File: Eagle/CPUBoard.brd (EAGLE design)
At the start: 100 x 80 mm, 33 parts, among them IC2 MAX232, IC3 MAX485CPA, J1 DISPLAY, J2 BUTTON_BOARD, J3 RELAY_BOARD, Q1 12.000MHz, X6 MKDSN1,5/3-5,08, X7 MKDSN1,5/3-5,08

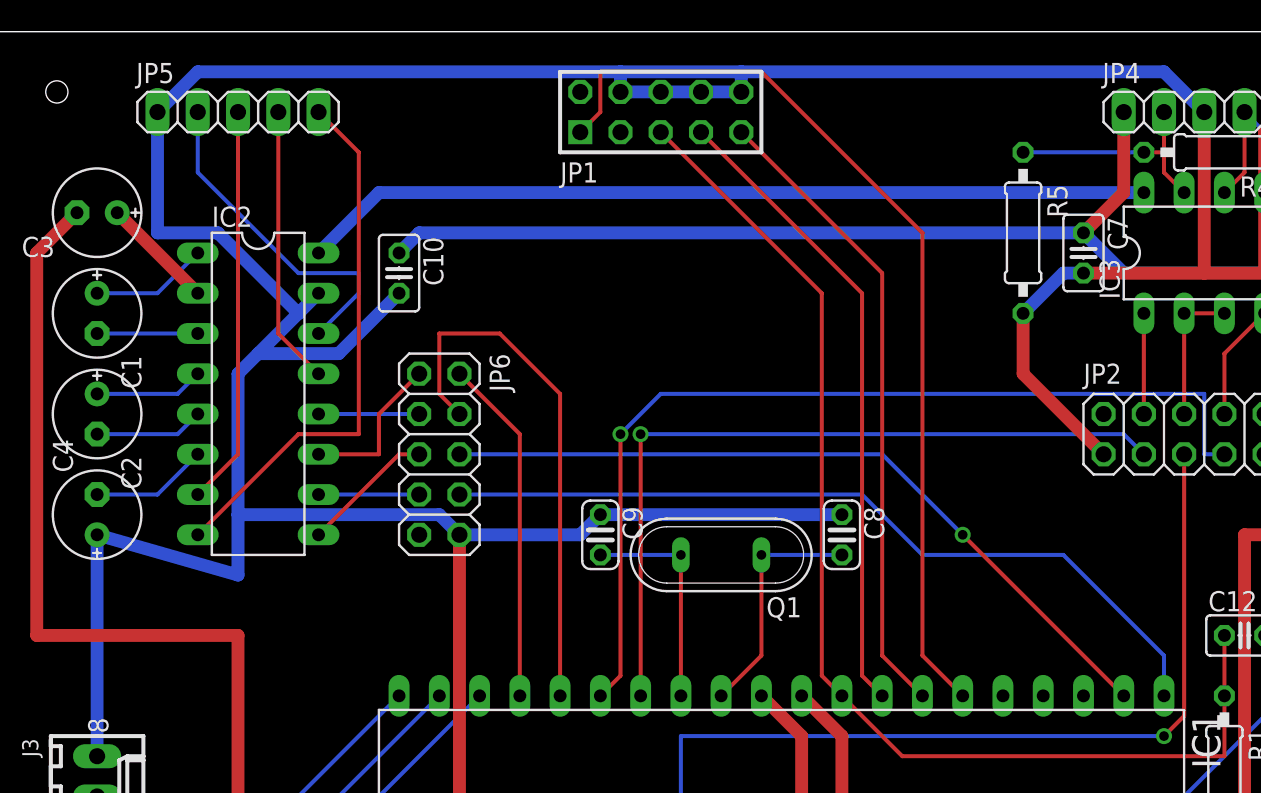
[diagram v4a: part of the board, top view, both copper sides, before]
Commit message: - wiring from/to MAX232 changed slightly
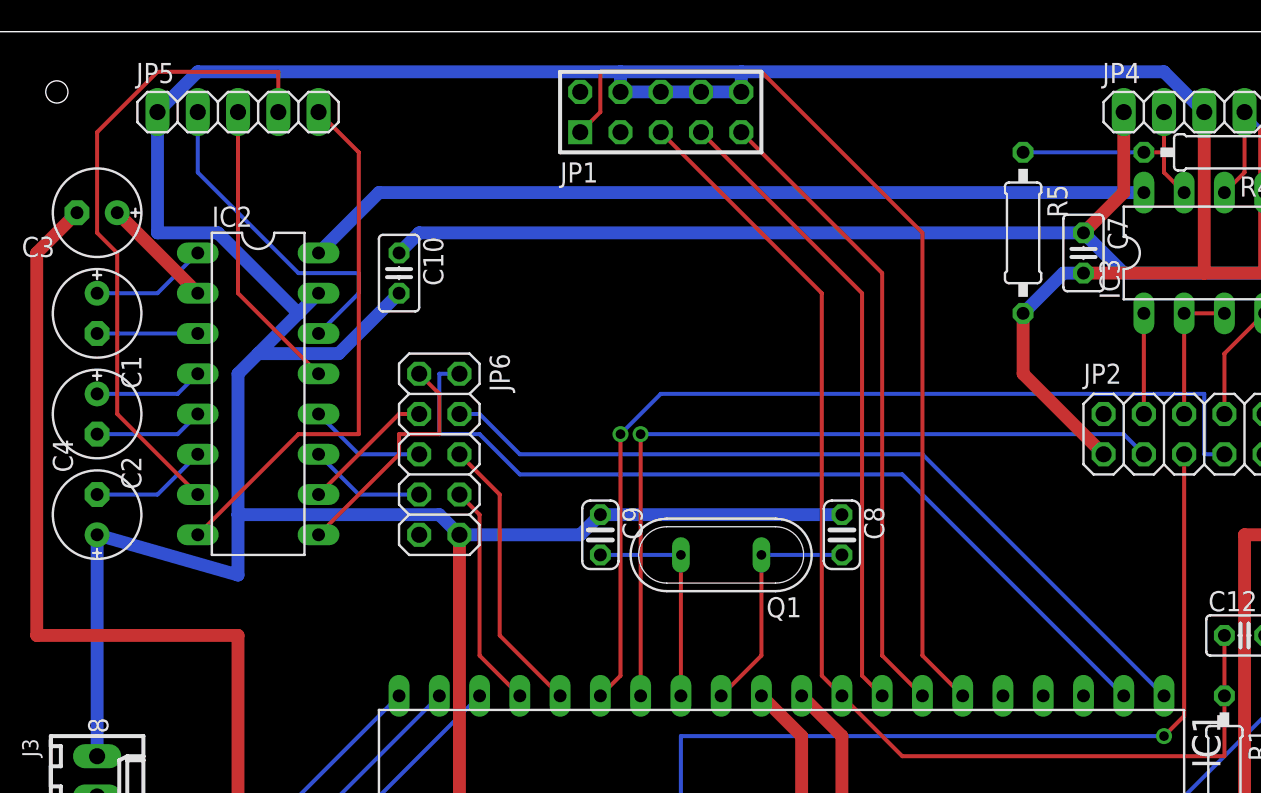
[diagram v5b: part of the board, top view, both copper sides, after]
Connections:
- removed net N$30: IC1.2, JP6.6
- removed net N$31: IC1.1, JP6.8
- new net N$22: IC1.16, JP6.6
- new net N$25: IC1.2, JP6.2
- net N$11: now also JP6.5; no longer JP6.3
- net N$16: now also IC1.1; no longer IC1.16
- net N$24: now also JP6.8; no longer JP6.2
- net N$28: now also JP6.1; no longer JP6.5
- net N$29: now also JP6.3; no longer JP6.7
- net N$4: now also JP6.7; no longer JP6.1
- net SER1_CTS: now also IC2.13; no longer IC2.7
- net SER1_RXD: now also IC2.7; no longer IC2.13
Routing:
- net N$25: track 0.00 -> 55.1 mm
- net N$31: track 51.2 -> 0.00 mm
- net N$30: track 48.2 -> 0.00 mm, vias 1 -> 0
- net SER1_RXD: track 17.6 -> 41.0 mm
- net N$16: track 33.9 -> 51.8 mm
- net N$22: track 0.00 -> 17.9 mm
- net N$24: track 21.9 -> 14.3 mm
- net N$28: track 8.45 -> 15.3 mm
- net SER1_CTS: track 25.2 -> 18.6 mm
- net N$4: track 9.94 -> 7.40 mm
- net N$29: track 6.35 -> 8.45 mm
- net N$11: track 6.35 -> 7.40 mm
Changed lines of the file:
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@@
 <wire x1="12.7" y1="74.93" x2="12.7" y2="71.12" width="0.254" layer="16"/>
 </signal>
-<signal name="SER1_RXD">
+<signal name="SER1_CTS">
 <contactref element="IC2" pad="13"/>
-<contactref element="JP5" pad="4"/>
-<wire x1="17.78" y1="60.96" x2="20.32" y2="58.42" width="0.254" layer="1"/>
-<wire x1="17.78" y1="74.93" x2="17.78" y2="60.96" width="0.254" layer="1"/>
+<contactref element="JP5" pad="3"/>
+<wire x1="15.24" y1="63.5" x2="20.32" y2="58.42" width="0.254" layer="1"/>
+<wire x1="15.24" y1="74.93" x2="15.24" y2="63.5" width="0.254" layer="1"/>
 </signal>
 <signal name="ENC_SCK">
@@
 <wire x1="38.1" y1="74.93" x2="38.1" y2="77.47" width="0.254" layer="1"/>
 <wire x1="36.83" y1="73.66" x2="38.1" y2="74.93" width="0.254" layer="1"/>
-</signal>
-<signal name="SER1_CTS">
-<contactref element="IC2" pad="7"/>
-<contactref element="JP5" pad="3"/>
-<wire x1="15.24" y1="53.34" x2="12.7" y2="50.8" width="0.254" layer="1"/>
-<wire x1="15.24" y1="74.93" x2="15.24" y2="53.34" width="0.254" layer="1"/>
 </signal>
 <signal name="LED_GREEN">
@@
 <signal name="N$4">
 <contactref element="IC2" pad="11"/>
-<contactref element="JP6" pad="1"/>
-<wire x1="24.13" y1="53.34" x2="20.32" y2="53.34" width="0.254" layer="1"/>
-<wire x1="24.13" y1="55.88" x2="24.13" y2="53.34" width="0.254" layer="1"/>
-<wire x1="26.67" y1="58.42" x2="24.13" y2="55.88" width="0.254" layer="1"/>
+<contactref element="JP6" pad="7"/>
+<wire x1="22.86" y1="50.8" x2="20.32" y2="53.34" width="0.254" layer="16"/>
+<wire x1="26.67" y1="50.8" x2="22.86" y2="50.8" width="0.254" layer="16"/>
 </signal>
 <signal name="N$11">
 <contactref element="IC2" pad="12"/>
-<contactref element="JP6" pad="3"/>
-<wire x1="26.67" y1="55.88" x2="20.32" y2="55.88" width="0.254" layer="16"/>
+<contactref element="JP6" pad="5"/>
+<wire x1="22.86" y1="53.34" x2="20.32" y2="55.88" width="0.254" layer="16"/>
+<wire x1="26.67" y1="53.34" x2="22.86" y2="53.34" width="0.254" layer="16"/>
 </signal>
 <signal name="N$13">
@@
 <wire x1="72.39" y1="72.39" x2="64.77" y2="72.39" width="0.254" layer="16"/>
 </signal>
-<signal name="N$16">
-<contactref element="IC1" pad="16"/>
-<contactref element="JP6" pad="4"/>
-<wire x1="35.56" y1="38.1" x2="35.56" y2="57.15" width="0.254" layer="1"/>
-<wire x1="35.56" y1="57.15" x2="31.75" y2="60.96" width="0.254" layer="1"/>
-<wire x1="31.75" y1="60.96" x2="27.94" y2="60.96" width="0.254" layer="1"/>
-<wire x1="27.94" y1="60.96" x2="27.94" y2="57.15" width="0.254" layer="1"/>
-<wire x1="27.94" y1="57.15" x2="29.21" y2="55.88" width="0.254" layer="1"/>
-</signal>
 <signal name="N$28">
 <contactref element="IC2" pad="9"/>
-<contactref element="JP6" pad="5"/>
+<contactref element="JP6" pad="1"/>
 <wire x1="25.4" y1="53.34" x2="20.32" y2="48.26" width="0.254" layer="1"/>
-<wire x1="26.67" y1="53.34" x2="25.4" y2="53.34" width="0.254" layer="1"/>
+<wire x1="25.4" y1="54.61" x2="25.4" y2="53.34" width="0.254" layer="1"/>
+<wire x1="27.94" y1="54.61" x2="25.4" y2="54.61" width="0.254" layer="1"/>
+<wire x1="27.94" y1="57.15" x2="27.94" y2="54.61" width="0.254" layer="1"/>
+<wire x1="26.67" y1="58.42" x2="27.94" y2="57.15" width="0.254" layer="1"/>
 </signal>
 <signal name="N$29">
 <contactref element="IC2" pad="10"/>
-<contactref element="JP6" pad="7"/>
-<wire x1="26.67" y1="50.8" x2="20.32" y2="50.8" width="0.254" layer="16"/>
-</signal>
-<signal name="N$30">
-<contactref element="IC1" pad="2"/>
-<contactref element="JP6" pad="6"/>
-<wire x1="60.96" y1="48.26" x2="71.12" y2="38.1" width="0.254" layer="1"/>
-<wire x1="55.88" y1="53.34" x2="60.96" y2="48.26" width="0.254" layer="16"/>
-<wire x1="29.21" y1="53.34" x2="55.88" y2="53.34" width="0.254" layer="16"/>
-<via x="60.96" y="48.26" extent="1-16" drill="0.6096"/>
-</signal>
-<signal name="N$31">
-<contactref element="IC1" pad="1"/>
-<contactref element="JP6" pad="8"/>
-<wire x1="73.66" y1="40.64" x2="73.66" y2="38.1" width="0.254" layer="16"/>
-<wire x1="67.31" y1="46.99" x2="73.66" y2="40.64" width="0.254" layer="16"/>
-<wire x1="58.42" y1="46.99" x2="67.31" y2="46.99" width="0.254" layer="16"/>
-<wire x1="54.61" y1="50.8" x2="58.42" y2="46.99" width="0.254" layer="16"/>
-<wire x1="29.21" y1="50.8" x2="54.61" y2="50.8" width="0.254" layer="16"/>
+<contactref element="JP6" pad="3"/>
+<wire x1="25.4" y1="55.88" x2="20.32" y2="50.8" width="0.254" layer="1"/>
+<wire x1="26.67" y1="55.88" x2="25.4" y2="55.88" width="0.254" layer="1"/>
 </signal>
 <signal name="N$24">
 <contactref element="IC1" pad="17"/>
-<contactref element="JP6" pad="2"/>
-<wire x1="33.02" y1="54.61" x2="33.02" y2="38.1" width="0.254" layer="1"/>
-<wire x1="29.21" y1="58.42" x2="33.02" y2="54.61" width="0.254" layer="1"/>
+<contactref element="JP6" pad="8"/>
+<wire x1="30.48" y1="40.64" x2="33.02" y2="38.1" width="0.254" layer="1"/>
+<wire x1="30.48" y1="49.53" x2="30.48" y2="40.64" width="0.254" layer="1"/>
+<wire x1="29.21" y1="50.8" x2="30.48" y2="49.53" width="0.254" layer="1"/>
 </signal>
 <signal name="N$19">
@@
 <contactref element="J1" pad="1"/>
 </signal>
+<signal name="SER1_RXD">
+<contactref element="IC2" pad="7"/>
+<contactref element="JP5" pad="4"/>
+<wire x1="7.62" y1="55.88" x2="12.7" y2="50.8" width="0.254" layer="1"/>
+<wire x1="7.62" y1="66.04" x2="7.62" y2="55.88" width="0.254" layer="1"/>
+<wire x1="6.35" y1="67.31" x2="7.62" y2="66.04" width="0.254" layer="1"/>
+<wire x1="6.35" y1="73.66" x2="6.35" y2="67.31" width="0.254" layer="1"/>
+<wire x1="10.16" y1="77.47" x2="6.35" y2="73.66" width="0.254" layer="1"/>
+<wire x1="17.78" y1="77.47" x2="10.16" y2="77.47" width="0.254" layer="1"/>
+<wire x1="17.78" y1="74.93" x2="17.78" y2="77.47" width="0.254" layer="1"/>
+</signal>
+<signal name="N$22">
+<contactref element="JP6" pad="6"/>
+<contactref element="IC1" pad="16"/>
+<wire x1="31.75" y1="41.91" x2="35.56" y2="38.1" width="0.254" layer="1"/>
+<wire x1="31.75" y1="50.8" x2="31.75" y2="41.91" width="0.254" layer="1"/>
+<wire x1="29.21" y1="53.34" x2="31.75" y2="50.8" width="0.254" layer="1"/>
+</signal>
+<signal name="N$16">
+<contactref element="IC1" pad="1"/>
+<contactref element="JP6" pad="4"/>
+<wire x1="58.42" y1="53.34" x2="73.66" y2="38.1" width="0.254" layer="16"/>
+<wire x1="33.02" y1="53.34" x2="58.42" y2="53.34" width="0.254" layer="16"/>
+<wire x1="30.48" y1="55.88" x2="33.02" y2="53.34" width="0.254" layer="16"/>
+<wire x1="29.21" y1="55.88" x2="30.48" y2="55.88" width="0.254" layer="16"/>
+</signal>
+<signal name="N$25">
+<contactref element="JP6" pad="2"/>
+<contactref element="IC1" pad="2"/>
+<wire x1="57.15" y1="52.07" x2="71.12" y2="38.1" width="0.254" layer="16"/>
+<wire x1="33.02" y1="52.07" x2="57.15" y2="52.07" width="0.254" layer="16"/>
+<wire x1="30.48" y1="54.61" x2="33.02" y2="52.07" width="0.254" layer="16"/>
+<wire x1="27.94" y1="54.61" x2="30.48" y2="54.61" width="0.254" layer="16"/>
+<wire x1="27.94" y1="58.42" x2="27.94" y2="54.61" width="0.254" layer="16"/>
+<wire x1="29.21" y1="58.42" x2="27.94" y2="58.42" width="0.254" layer="16"/>
+</signal>
 </signals>

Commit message: - another fix for the TWI pins, hopefully the last one!
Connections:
- net SCL: now also J1.3; no longer J1.2
- net SDA: now also J1.2; no longer J1.3
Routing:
- net GND: track 393.2 -> 400.4 mm
- net N$14: track 60.0 -> 64.3 mm
- net SCL: track 21.2 -> 23.9 mm
- net SDA: track 23.7 -> 24.7 mm
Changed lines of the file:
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@@
 <wire x1="52.07" y1="21.59" x2="50.8" y2="22.86" width="0.8128" layer="1"/>
 <wire x1="52.07" y1="17.78" x2="52.07" y2="21.59" width="0.8128" layer="1"/>
-<wire x1="50.8" y1="35.56" x2="48.26" y2="38.1" width="0.8128" layer="1"/>
-<wire x1="50.8" y1="22.86" x2="50.8" y2="29.21" width="0.8128" layer="1"/>
-<wire x1="50.8" y1="29.21" x2="50.8" y2="35.56" width="0.8128" layer="1"/>
 <wire x1="46.99" y1="19.05" x2="45.72" y2="17.78" width="0.8128" layer="16"/>
 <wire x1="50.8" y1="19.05" x2="46.99" y2="19.05" width="0.8128" layer="16"/>
@@
 <wire x1="36.83" y1="48.26" x2="38.1" y2="49.53" width="0.8128" layer="16"/>
 <wire x1="29.21" y1="48.26" x2="36.83" y2="48.26" width="0.8128" layer="16"/>
-<wire x1="38.1" y1="49.53" x2="53.34" y2="49.53" width="0.8128" layer="16"/>
+<wire x1="38.1" y1="49.53" x2="43.18" y2="49.53" width="0.8128" layer="16"/>
+<wire x1="43.18" y1="49.53" x2="53.34" y2="49.53" width="0.8128" layer="16"/>
 <wire x1="15.24" y1="58.42" x2="16.51" y2="59.69" width="0.8128" layer="16"/>
 <wire x1="16.51" y1="59.69" x2="19.05" y2="62.23" width="0.8128" layer="16"/>
@@
 <contactref element="J3" pad="8"/>
 <wire x1="6.35" y1="34.29" x2="6.35" y2="48.26" width="0.8128" layer="16"/>
-<wire x1="29.21" y1="48.26" x2="29.21" y2="29.21" width="0.8128" layer="1"/>
-<wire x1="29.21" y1="29.21" x2="29.21" y2="6.35" width="0.8128" layer="1"/>
 <wire x1="45.72" y1="10.16" x2="49.53" y2="6.35" width="0.8128" layer="1"/>
 <wire x1="45.72" y1="17.78" x2="45.72" y2="10.16" width="0.8128" layer="1"/>
@@
 <wire x1="21.59" y1="59.69" x2="25.4" y2="63.5" width="0.8128" layer="16"/>
 <wire x1="16.51" y1="59.69" x2="21.59" y2="59.69" width="0.8128" layer="16"/>
-<wire x1="29.21" y1="29.21" x2="50.8" y2="29.21" width="0.8128" layer="1"/>
 <wire x1="67.31" y1="64.77" x2="64.77" y2="62.23" width="0.8128" layer="16"/>
 <wire x1="68.58" y1="64.77" x2="67.31" y2="64.77" width="0.8128" layer="16"/>
@@
 <wire x1="46.99" y1="77.47" x2="39.37" y2="77.47" width="0.8128" layer="16"/>
 <wire x1="39.37" y1="77.47" x2="39.37" y2="76.2" width="0.8128" layer="16"/>
-<wire x1="50.8" y1="29.21" x2="50.8" y2="30.48" width="0" layer="19" extent="1-1"/>
+<wire x1="50.8" y1="22.86" x2="50.8" y2="30.48" width="0.8128" layer="1"/>
+<wire x1="50.8" y1="30.48" x2="48.26" y2="30.48" width="0.8128" layer="1"/>
+<wire x1="48.26" y1="38.1" x2="48.26" y2="30.48" width="0.8128" layer="1"/>
+<wire x1="48.26" y1="30.48" x2="20.32" y2="30.48" width="0.8128" layer="1"/>
+<wire x1="20.32" y1="30.48" x2="20.32" y2="16.51" width="0.8128" layer="1"/>
+<wire x1="20.32" y1="16.51" x2="29.21" y2="7.62" width="0.8128" layer="1"/>
+<wire x1="29.21" y1="7.62" x2="29.21" y2="6.35" width="0.8128" layer="1"/>
+<wire x1="48.26" y1="44.45" x2="48.26" y2="38.1" width="0.8128" layer="16"/>
+<wire x1="43.18" y1="49.53" x2="48.26" y2="44.45" width="0.8128" layer="16"/>
 </signal>
 <signal name="N$1">
@@
 <wire x1="92.71" y1="63.5" x2="92.735" y2="63.5211" width="0.254" layer="16"/>
 <wire x1="81.28" y1="27.94" x2="78.74" y2="27.94" width="0.8128" layer="1"/>
-<wire x1="78.74" y1="27.94" x2="77.47" y2="27.94" width="0.254" layer="1"/>
+<wire x1="78.74" y1="27.94" x2="77.47" y2="27.94" width="0.8128" layer="1"/>
 <wire x1="53.34" y1="35.56" x2="53.34" y2="30.48" width="0.8128" layer="1"/>
 <wire x1="53.34" y1="30.48" x2="53.34" y2="27.94" width="0.8128" layer="1"/>
@@
 <contactref element="IC1" pad="15"/>
 <contactref element="JP2" pad="7"/>
-<wire x1="39.37" y1="39.37" x2="38.1" y2="38.1" width="0.254" layer="1"/>
-<wire x1="39.37" y1="54.61" x2="39.37" y2="39.37" width="0.254" layer="1"/>
-<wire x1="41.91" y1="57.15" x2="39.37" y2="54.61" width="0.254" layer="16"/>
-<wire x1="76.2" y1="57.15" x2="41.91" y2="57.15" width="0.254" layer="16"/>
+<wire x1="35.56" y1="40.64" x2="38.1" y2="38.1" width="0.254" layer="1"/>
+<wire x1="35.56" y1="54.61" x2="35.56" y2="40.64" width="0.254" layer="1"/>
+<wire x1="38.1" y1="57.15" x2="35.56" y2="54.61" width="0.254" layer="16"/>
+<wire x1="76.2" y1="57.15" x2="38.1" y2="57.15" width="0.254" layer="16"/>
 <wire x1="76.2" y1="53.34" x2="76.2" y2="57.15" width="0.254" layer="16"/>
 <wire x1="77.47" y1="53.34" x2="76.2" y2="53.34" width="0.254" layer="16"/>
-<via x="39.37" y="54.61" extent="1-16" drill="0.6096"/>
+<via x="35.56" y="54.61" extent="1-16" drill="0.6096"/>
 </signal>
 <signal name="SCL">
@@
 <wire x1="26.67" y1="16.51" x2="26.67" y2="21.59" width="0.254" layer="1"/>
 <wire x1="25.4" y1="15.24" x2="26.67" y2="16.51" width="0.254" layer="1"/>
-<contactref element="J1" pad="2"/>
-<wire x1="25.4" y1="15.24" x2="34.29" y2="6.35" width="0.254" layer="16"/>
+<contactref element="J1" pad="3"/>
+<wire x1="31.75" y1="15.24" x2="31.75" y2="6.35" width="0.254" layer="16"/>
+<wire x1="25.4" y1="15.24" x2="31.75" y2="15.24" width="0.254" layer="16"/>
 </signal>
 <signal name="SDA">
@@
 <wire x1="27.94" y1="20.32" x2="26.67" y2="20.32" width="0.254" layer="16"/>
 <wire x1="30.48" y1="22.86" x2="27.94" y2="20.32" width="0.254" layer="16"/>
-<contactref element="J1" pad="3"/>
-<wire x1="30.48" y1="7.62" x2="31.75" y2="6.35" width="0.254" layer="1"/>
-<wire x1="30.48" y1="22.86" x2="30.48" y2="7.62" width="0.254" layer="1"/>
+<contactref element="J1" pad="2"/>
+<wire x1="30.48" y1="10.16" x2="34.29" y2="6.35" width="0.254" layer="1"/>
+<wire x1="30.48" y1="22.86" x2="30.48" y2="10.16" width="0.254" layer="1"/>
 </signal>
 <signal name="N$12">
